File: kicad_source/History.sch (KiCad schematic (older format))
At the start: 0 parts

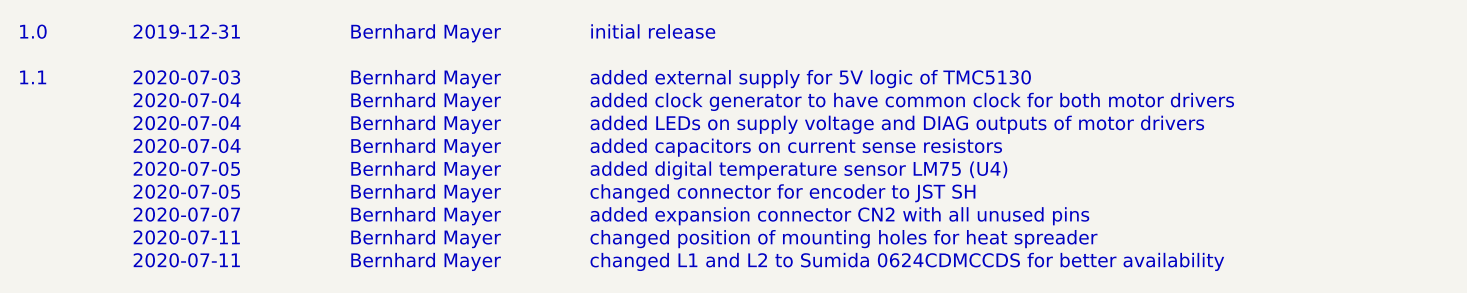
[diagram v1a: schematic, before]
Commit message: corrected links and titles, generated schematic pdf and net list
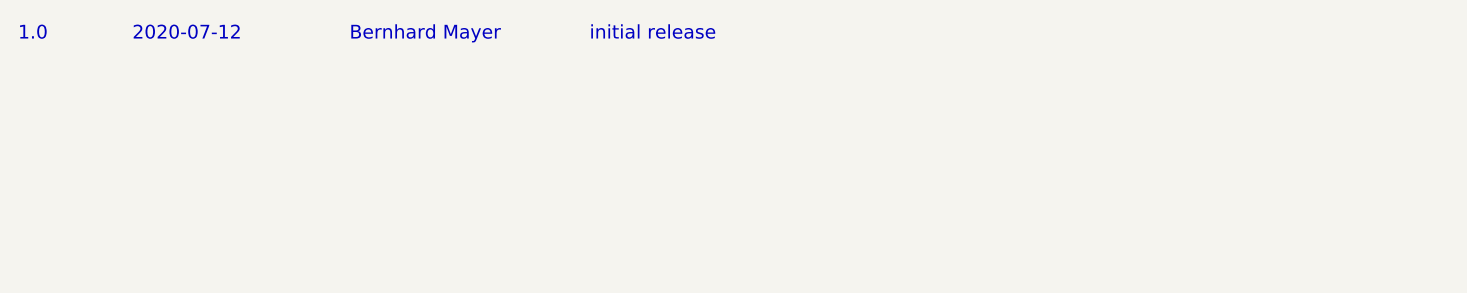
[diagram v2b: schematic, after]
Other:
- note added: "2020-07-12"
- note removed: "1.1"
- note removed: "2019-12-31"
- note removed: "2020-07-03"
- note removed: "2020-07-04"
- note removed: "2020-07-05"
- note removed: "2020-07-07"
- note removed: "2020-07-11"
- note removed: "added LEDs on supply voltage and DIAG outputs of motor drivers"
- note removed: "added capacitors on current sense resistors"
- note removed: "added clock generator to have common clock for both motor drivers"
- note removed: "added digital temperature sensor LM75 (U4)"
- note removed: "added expansion connector CN2 with all unused pins"
- note removed: "added external supply for 5V logic of TMC5130"
- note removed: "changed L1 and L2 to Sumida 0624CDMCCDS for better availability"
- note removed: "changed connector for encoder to JST SH"
- note removed: "changed position of mounting holes for heat spreader"
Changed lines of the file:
@@
 encoding utf-8
 Sheet 6 6
-Title "StepperMotorFeatherWing"
-Date "2020-07-11"
+Title "StepperMotorMKRShield"
+Date "2020-07-12"
 Rev "1.1"
 Comp "generationmake"
@@
 1.0
 Text Notes 1350 900  0    60   ~ 0
-2019-12-31
+2020-07-12
 Text Notes 2300 900  0    60   ~ 0
 Bernhard Mayer
 Text Notes 3350 900  0    60   ~ 0
 initial release
-Text Notes 850  1100 0    60   ~ 0
-1.1
-Text Notes 1350 1100 0    60   ~ 0
-2020-07-03
-Text Notes 2300 1100 0    60   ~ 0
-Bernhard Mayer
-Text Notes 3350 1100 0    60   ~ 0
-added external supply for 5V logic of TMC5130
-Text Notes 1350 1200 0    60   ~ 0
-2020-07-04
-Text Notes 2300 1200 0    60   ~ 0
-Bernhard Mayer
-Text Notes 3350 1200 0    60   ~ 0
-added clock generator to have common clock for both motor drivers
-Text Notes 1350 1300 0    60   ~ 0
-2020-07-04
-Text Notes 2300 1300 0    60   ~ 0
-Bernhard Mayer
-Text Notes 3350 1300 0    60   ~ 0
-added LEDs on supply voltage and DIAG outputs of motor drivers
-Text Notes 1350 1400 0    60   ~ 0
-2020-07-04
-Text Notes 2300 1400 0    60   ~ 0
-Bernhard Mayer
-Text Notes 3350 1400 0    60   ~ 0
-added capacitors on current sense resistors
-Text Notes 1350 1500 0    60   ~ 0
-2020-07-05
-Text Notes 2300 1500 0    60   ~ 0
-Bernhard Mayer
-Text Notes 3350 1500 0    60   ~ 0
-added digital temperature sensor LM75 (U4)
-Text Notes 1350 1600 0    60   ~ 0
-2020-07-05
-Text Notes 2300 1600 0    60   ~ 0
-Bernhard Mayer
-Text Notes 3350 1600 0    60   ~ 0
-changed connector for encoder to JST SH
-Text Notes 1350 1700 0    60   ~ 0
-2020-07-07
-Text Notes 2300 1700 0    60   ~ 0
-Bernhard Mayer
-Text Notes 3350 1700 0    60   ~ 0
-added expansion connector CN2 with all unused pins
-Text Notes 1350 1800 0    60   ~ 0
-2020-07-11
-Text Notes 2300 1800 0    60   ~ 0
-Bernhard Mayer
-Text Notes 3350 1800 0    60   ~ 0
-changed position of mounting holes for heat spreader
-Text Notes 1350 1900 0    60   ~ 0
-2020-07-11
-Text Notes 2300 1900 0    60   ~ 0
-Bernhard Mayer
-Text Notes 3350 1900 0    60   ~ 0
-changed L1 and L2 to Sumida 0624CDMCCDS for better availability
 $EndSCHEMATC
